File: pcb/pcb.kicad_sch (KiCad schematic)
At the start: 30 parts, among them J1 Screw_Terminal_01x03, J2 PWR_IN, J3 Screw_Terminal_01x03, J4 Screw_Terminal_01x03, J5 Screw_Terminal_01x03, J6 Screw_Terminal_01x03, J7 Screw_Terminal_01x03, J8 RELE_OUT, J9 PWR_IN_RELE, K2 SANYOU_SRD_Form_C, Q1 2N3904, U1 ESP32-DEVKITC, U2 PC817

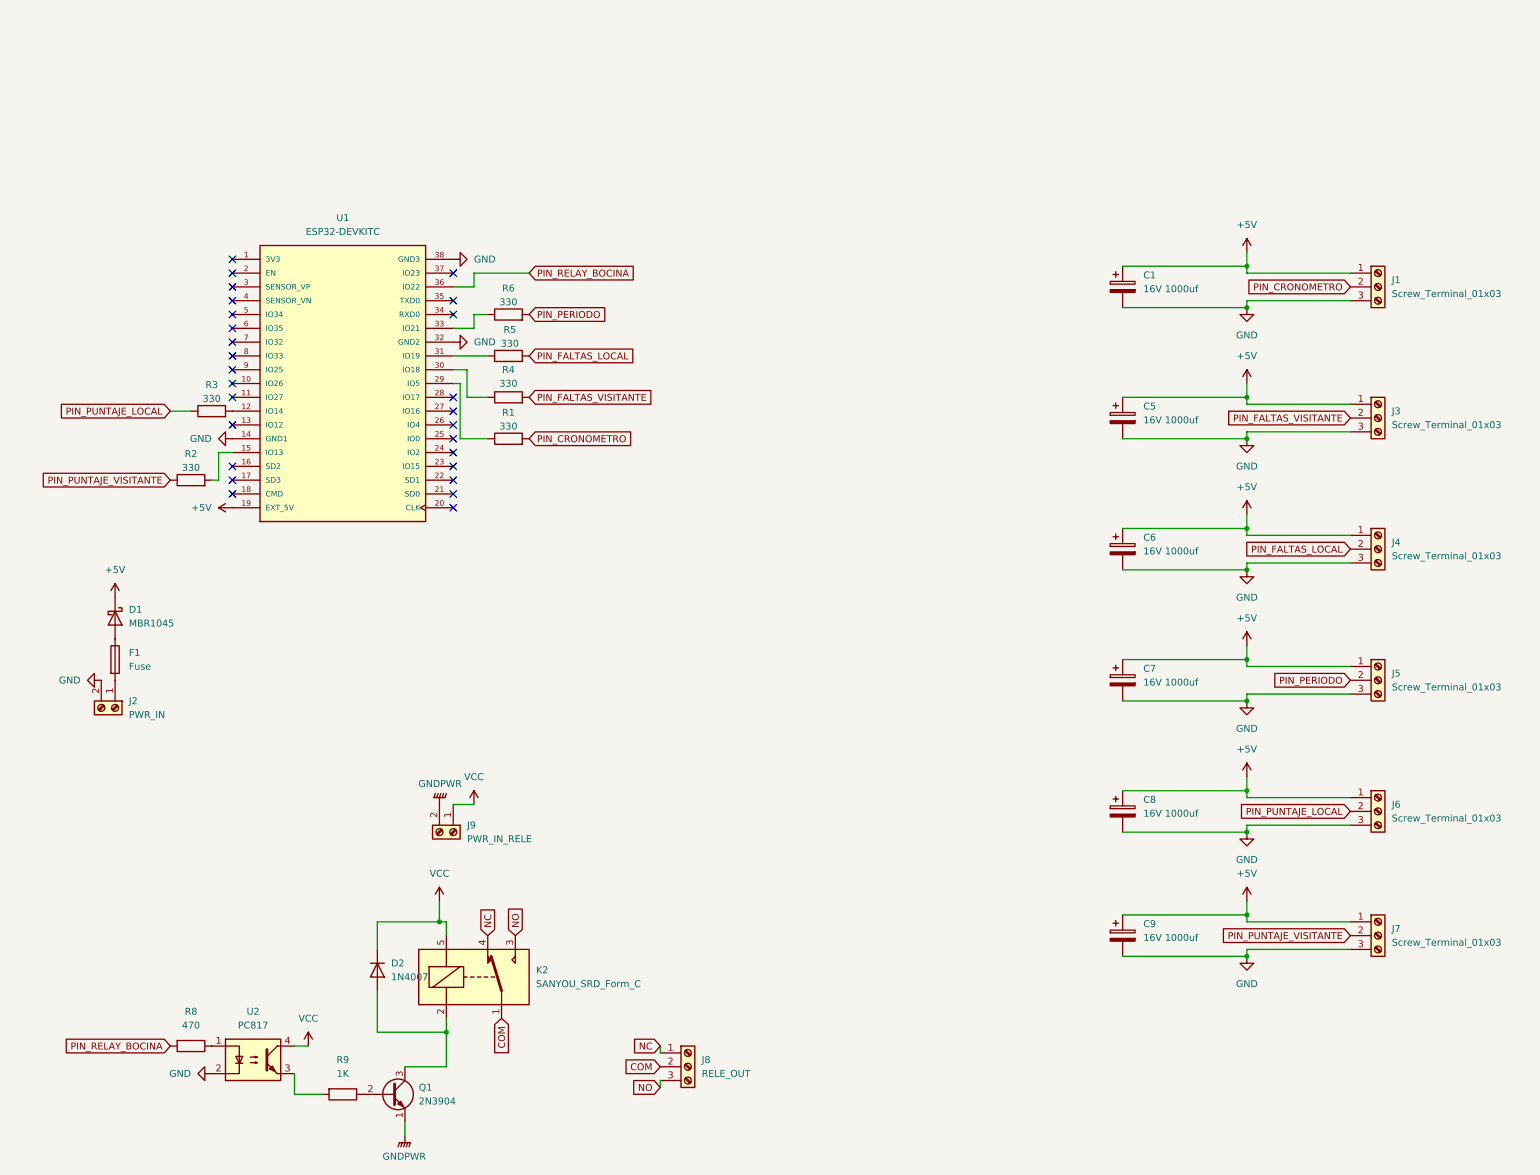
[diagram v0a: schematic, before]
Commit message: refactor: optimize power efficiency and reduce PCB footprint
Replace series protection diode with P-Channel MOSFET (AOD4185) to minimize voltage drop.

Migrate from ESP32-DevKitC to Wemos D1 Mini (ESP8266) for cost and size reduction.

Replace mechanical relay with N-Channel MOSFET for silent and efficient buzzer control.

Update schematics and PCB layout accordingly.
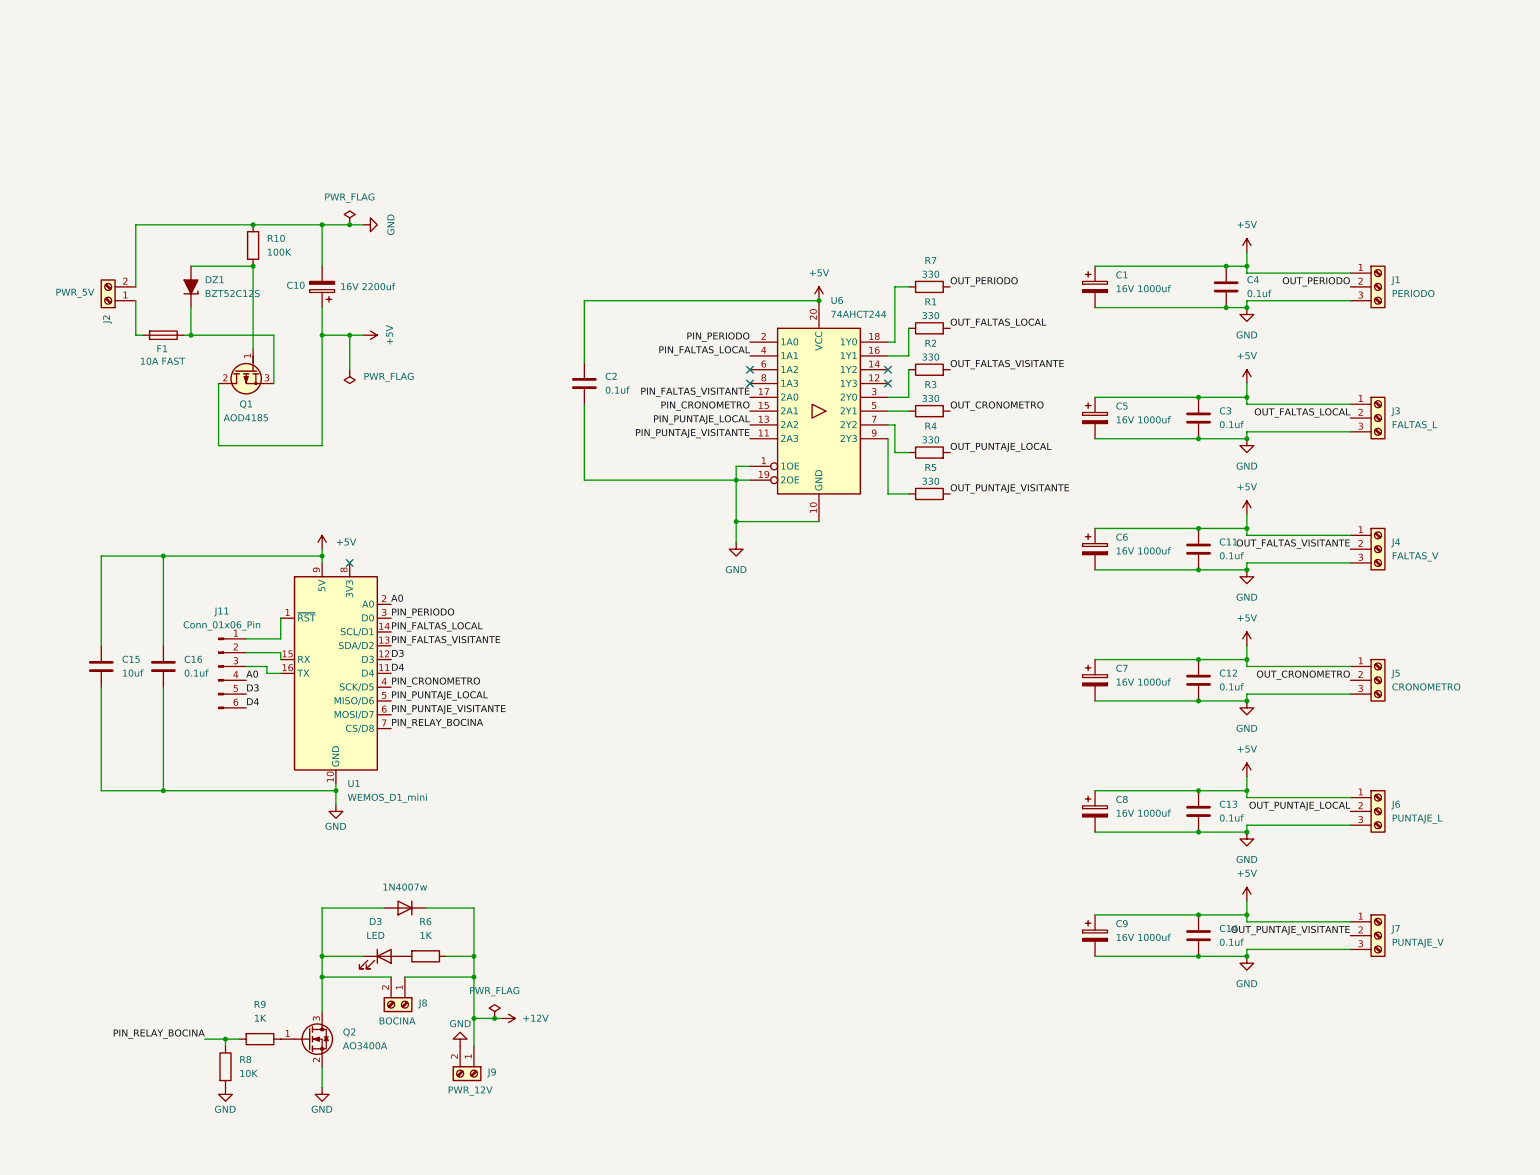
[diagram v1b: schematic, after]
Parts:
- removed D1: MBR1045, Package_TO_SOT_THT:TO-220-2_Vertical, symbol Device:D_Schottky
- removed J8: RELE_OUT, TerminalBlock:TerminalBlock_Altech_AK300-3_P5.00mm, symbol Connector:Screw_Terminal_01x03
- removed K2: SANYOU_SRD_Form_C, Relay_THT:Relay_SPDT_SANYOU_SRD_Series_Form_C, symbol Relay:SANYOU_SRD_Form_C
- removed Q1: 2N3904, Package_TO_SOT_THT:TO-92_Inline, symbol Transistor_BJT:2N3904
- removed U1: ESP32-DEVKITC, ESP32-DEVKITC:MODULE_ESP32-DEVKITC, symbol ESP32-DEVKITC:ESP32-DEVKITC
- removed U2: PC817, Package_DIP:DIP-4_W7.62mm, symbol Isolator:PC817
- added C10: 16V 2200uf, Capacitor_THT:CP_Radial_D10.0mm_P5.00mm, symbol Device:C_Polarized
- added C11, C12, C13, C14, C16, C2, C3, C4: 0.1uf, PCM_Capacitor_SMD_AKL:C_0805_2012Metric, symbol PCM_Capacitor_AKL:C_0805
- added C15: 10uf, PCM_Capacitor_SMD_AKL:C_0805_2012Metric, symbol PCM_Capacitor_AKL:C_0805
- added D3: LED, LED_SMD:LED_0805_2012Metric_Pad1.15x1.40mm_HandSolder, symbol Device:LED
- added DZ1: BZT52C12S, PCM_Diode_SMD_AKL:D_SOD-323, symbol PCM_Diode_Zener_AKL:BZT52C12S
- added J11: Conn_01x06_Pin, Connector_PinHeader_2.54mm:PinHeader_1x06_P2.54mm_Vertical, symbol Connector:Conn_01x06_Pin
- added J8: BOCINA, TerminalBlock:TerminalBlock_Altech_AK300-2_P5.00mm, symbol Connector:Screw_Terminal_01x02
- added Q1: AOD4185, PCM_Package_TO_SOT_SMD_AKL:TO-252-2, symbol PCM_Transistor_MOSFET_AKL:AOD4185
- added Q2: AO3400A, Package_TO_SOT_SMD:SOT-23, symbol Transistor_FET:AO3400A
- added R10: 100K, Resistor_SMD:R_1206_3216Metric_Pad1.30x1.75mm_HandSolder, symbol Device:R
- added R7: 330, Resistor_SMD:R_1206_3216Metric_Pad1.30x1.75mm_HandSolder, symbol Device:R
- added U1: WEMOS_D1_mini, RF_Module:WEMOS_D1_mini_light, symbol RF_Module:WEMOS_D1_mini
- added U6: 74AHCT244, Package_SO:SO-20_12.8x7.5mm_P1.27mm, symbol 74xx:74AHCT244
- C1, C5, C6, C7, C8, C9: footprint Capacitor_THT:CP_Radial_D6.3mm_P2.50mm -> Capacitor_THT:CP_Radial_D10.0mm_P5.00mm
- D2: value 1N4007 -> 1N4007w; footprint Diode_THT:D_DO-41_SOD81_P10.16mm_Horizontal -> Diode_SMD:D_SOD-123
- F1: value Fuse -> 10A FAST; footprint Fuse:Fuse_1206_3216Metric_Pad1.42x1.75mm_HandSolder -> Fuse:Fuse_0603_1608Metric_Pad1.05x0.95mm_HandSolder
- J1: value Screw_Terminal_01x03 -> PERIODO
- J2: value PWR_IN -> PWR_5V
- J3: value Screw_Terminal_01x03 -> FALTAS_L
- J4: value Screw_Terminal_01x03 -> FALTAS_V
- J5: value Screw_Terminal_01x03 -> CRONOMETRO
- J6: value Screw_Terminal_01x03 -> PUNTAJE_L
- J7: value Screw_Terminal_01x03 -> PUNTAJE_V
- J9: value PWR_IN_RELE -> PWR_12V
- R6: value 330 -> 1K
- R8: value 470 -> 10K
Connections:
- net GNDPWR is gone; now on net GND: J9.2 (Pin_2)
- net VCC is gone; now on net +12V: D2.1 (K), J9.1 (Pin_1)
- net +5V: now also C10.1, C11.1, C12.1, C13.1, C14.1, C15.1, C16.1, C2.1, C3.1, C4.1, Q1.2 (D), U1.9 (5V), U6.20 (VCC)
- net GND: now also R8.2, C10.2, C11.2, C12.2, C13.2, C14.2, C15.2, C16.2, C2.2, C3.2, C4.2, Q2.2 (S), R10.1, U1.10 (GND), U6.1 (1OE), U6.10 (GND), U6.19 (2OE)
- net PIN_CRONOMETRO: now also U1.4 (SCK/D5), U6.15 (2A1); no longer J1.2 (Pin_2), R1.2
- net PIN_FALTAS_LOCAL: now also U1.14 (SCL/D1), U6.4 (1A1); no longer J4.2 (Pin_2), R5.2
- net PIN_FALTAS_VISITANTE: now also U1.13 (SDA/D2), U6.17 (2A0); no longer J3.2 (Pin_2), R4.2
- net PIN_PERIODO: now also U1.3 (D0), U6.2 (1A0); no longer J5.2 (Pin_2), R6.2
- net PIN_PUNTAJE_LOCAL: now also U1.5 (MISO/D6), U6.13 (2A2); no longer J6.2 (Pin_2), R3.1
- net PIN_PUNTAJE_VISITANTE: now also U1.6 (MOSI/D7), U6.11 (2A3); no longer J7.2 (Pin_2), R2.1
- net PIN_RELAY_BOCINA: now also R8.1, R9.2, U1.7 (CS/D8); no longer R8.2
- net at R9.1: now also Q2.1 (G)
- net at D2.2 (A): now also D3.1 (K), J8.2 (Pin_2), Q2.3 (D)
- net at F1.1: now also DZ1.1 (K), Q1.3 (S)
- net at R4.1: now also U6.7 (2Y2)
- net at R1.1: now also U6.16 (1Y1)
- net at R5.1: now also U6.9 (2Y3)
- net OUT_CRONOMETRO: now reaches R3.2
- net OUT_CRONOMETRO: now also J5.2 (Pin_2)
- net OUT_FALTAS_VISITANTE: now reaches R2.2
- net OUT_FALTAS_VISITANTE: now also J4.2 (Pin_2)
- net +12V: now reaches R6.1
- net +12V: now also J8.1 (Pin_1)
- new net: DZ1.2 (A), Q1.1 (G), R10.2
- new net: D3.2 (A), R6.2
- new net: R2.1, U6.3 (2Y0)
- new net: J11.1 (Pin_1), U1.1 (~{RST})
- new net: J11.2 (Pin_2), U1.15 (RX)
- new net: J11.3 (Pin_3), U1.16 (TX)
- new net: R3.1, U6.5 (2Y1)
- new net: R7.1, U6.18 (1Y0)
- new net A0: J11.4 (Pin_4), U1.2 (A0)
- new net D3: J11.5 (Pin_5), U1.12 (D3)
- new net D4: J11.6 (Pin_6), U1.11 (D4)
- new net OUT_FALTAS_LOCAL: J3.2 (Pin_2), R1.2
- new net OUT_PERIODO: J1.2 (Pin_2), R7.2
- new net OUT_PUNTAJE_LOCAL: J6.2 (Pin_2), R4.2
- new net OUT_PUNTAJE_VISITANTE: J7.2 (Pin_2), R5.2
- no-connect marks 27 -> 5
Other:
- moved on the sheet: C1, C5, C6, C7, C8, C9, F1, J2, J9, R8, R9

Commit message: feat(pcb): Actualizar diseño y eliminar esquemático obsoleto
- Reemplaza conector de 6 por 5 pines en el esquemático.

- Regenera el layout del PCB y actualiza el ruteado.

- Añade nuevo ancho de pista de 0.35mm en la configuración.

- Elimina el archivo de esquemático no utilizado 'untitled.kicad_sch'.
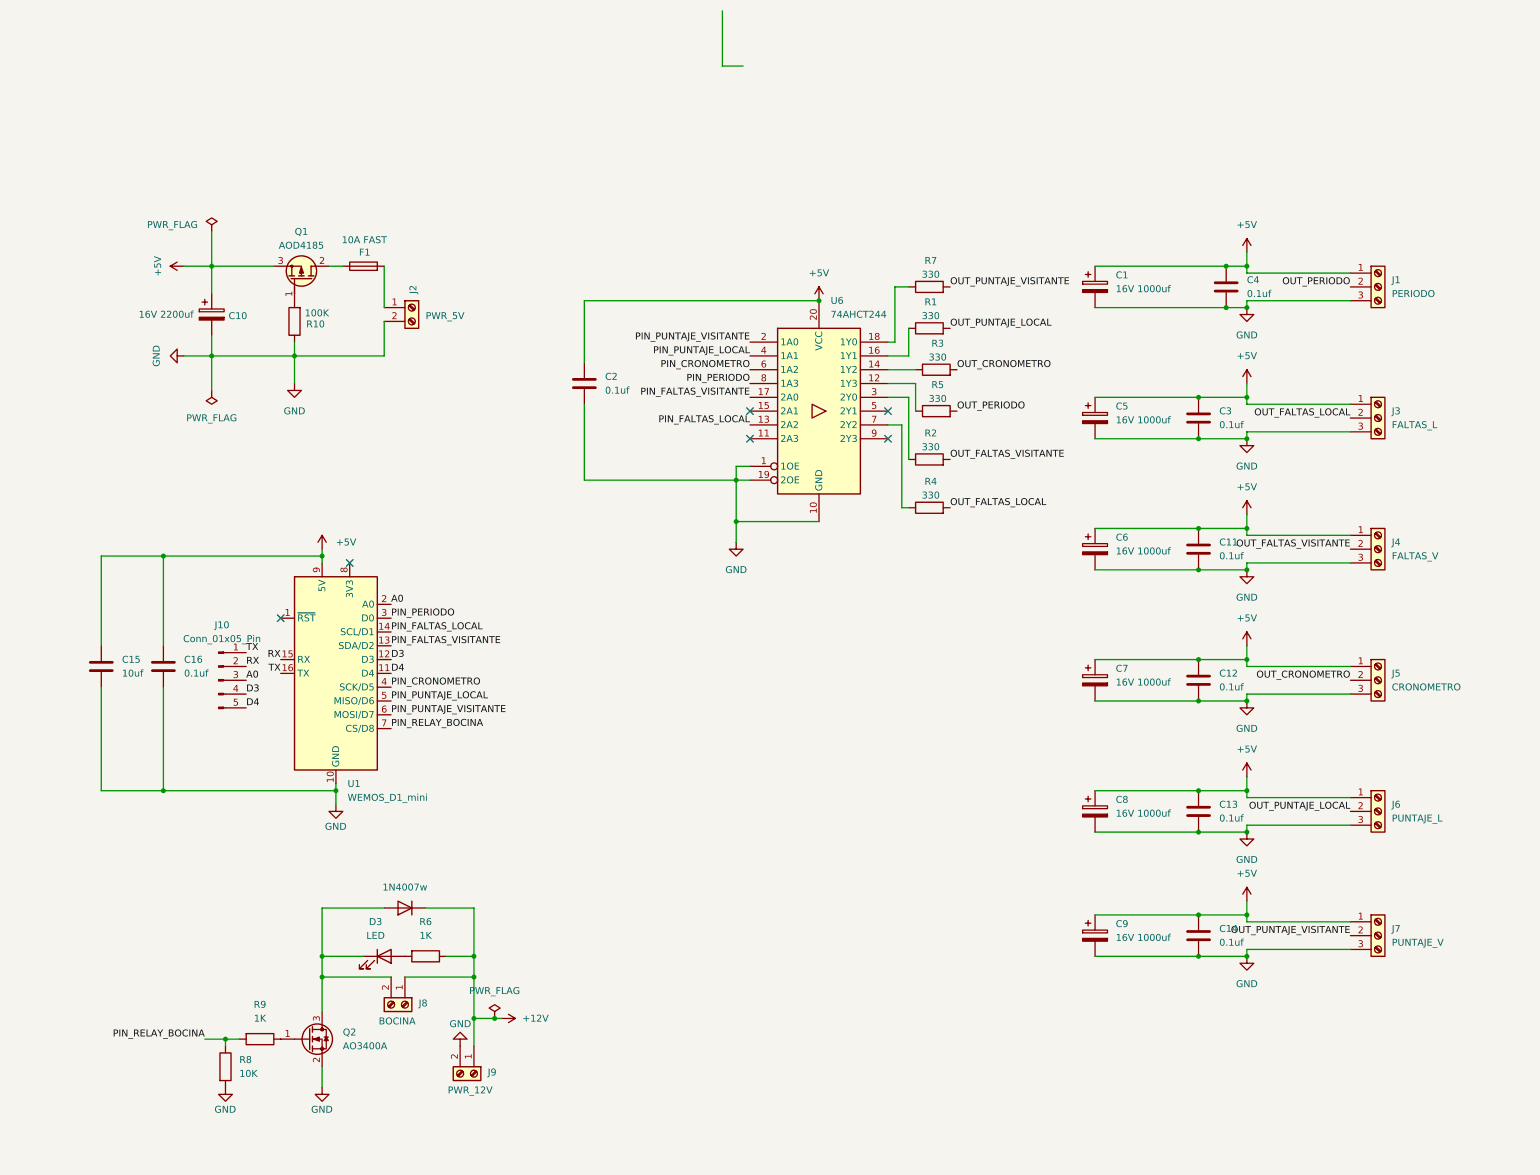
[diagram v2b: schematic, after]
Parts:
- removed DZ1: BZT52C12S, PCM_Diode_SMD_AKL:D_SOD-323, symbol PCM_Diode_Zener_AKL:BZT52C12S
- removed J11: Conn_01x06_Pin, Connector_PinHeader_2.54mm:PinHeader_1x06_P2.54mm_Vertical, symbol Connector:Conn_01x06_Pin
- added J10: Conn_01x05_Pin, Connector_PinHeader_2.54mm:PinHeader_1x05_P2.54mm_Vertical, symbol Connector:Conn_01x05_Pin
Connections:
- net +5V: now also Q1.3 (S); no longer Q1.2 (D)
- net A0: now also J10.3 (Pin_3)
- net D3: now also J10.4 (Pin_4)
- net D4: now also J10.5 (Pin_5)
- net OUT_FALTAS_LOCAL: now also R4.2; no longer R1.2
- net OUT_PERIODO: now also R5.2; no longer R7.2
- net OUT_PUNTAJE_LOCAL: now also R1.2; no longer R4.2
- net OUT_PUNTAJE_VISITANTE: now also R7.2; no longer R5.2
- net PIN_CRONOMETRO: now also U6.6 (1A2); no longer U6.15 (2A1)
- net PIN_FALTAS_LOCAL: now also U6.13 (2A2); no longer U6.4 (1A1)
- net PIN_PERIODO: now also U6.8 (1A3); no longer U6.2 (1A0)
- net PIN_PUNTAJE_LOCAL: now also U6.4 (1A1); no longer U6.13 (2A2)
- net PIN_PUNTAJE_VISITANTE: now also U6.2 (1A0); no longer U6.11 (2A3)
- net at F1.1: now also Q1.2 (D); no longer Q1.3 (S)
- net at R5.1: now also U6.12 (1Y3); no longer U6.9 (2Y3)
- net RX: now reaches U1.15 (RX)
- net RX: now also J10.2 (Pin_2)
- net TX: now reaches U1.16 (TX)
- net TX: now also J10.1 (Pin_1)
- net at R3.1: now also U6.14 (1Y2); no longer U6.5 (2Y1)
- no-connect marks 5 -> 6
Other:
- moved on the sheet: C10, F1, J2, Q1, R10, R2, R3, R4, R5
